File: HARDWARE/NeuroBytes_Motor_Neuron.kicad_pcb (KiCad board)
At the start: 2 copper layers, 51.2 x 28.4 mm, 28 parts, among them P1 JST_GH_4POS, P2 JST_GH_4POS, P3 JST_GH_4POS, P4 SERVO_CONN, P5 SERVO_CONN, P6 JST_GH_5-pos, Q1 MMBT3904, Q2 MMBT3904, Q3 MMBT3904, SW1 SW_PUSH, U1 STM32L011Gx, U2 LD3985G33R

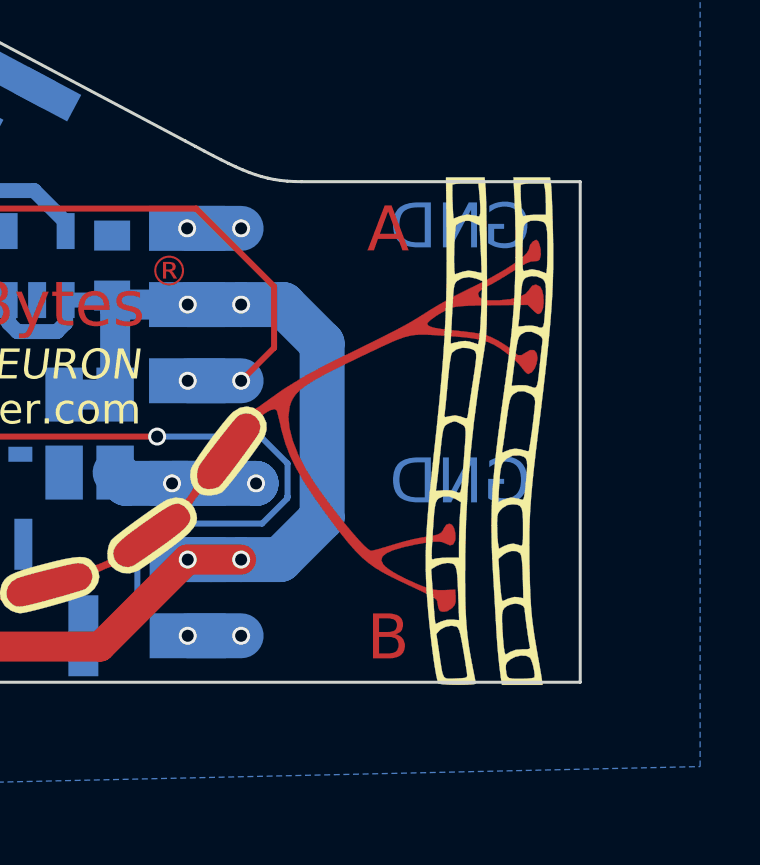
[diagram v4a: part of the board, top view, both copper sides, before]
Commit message: updated servo labels
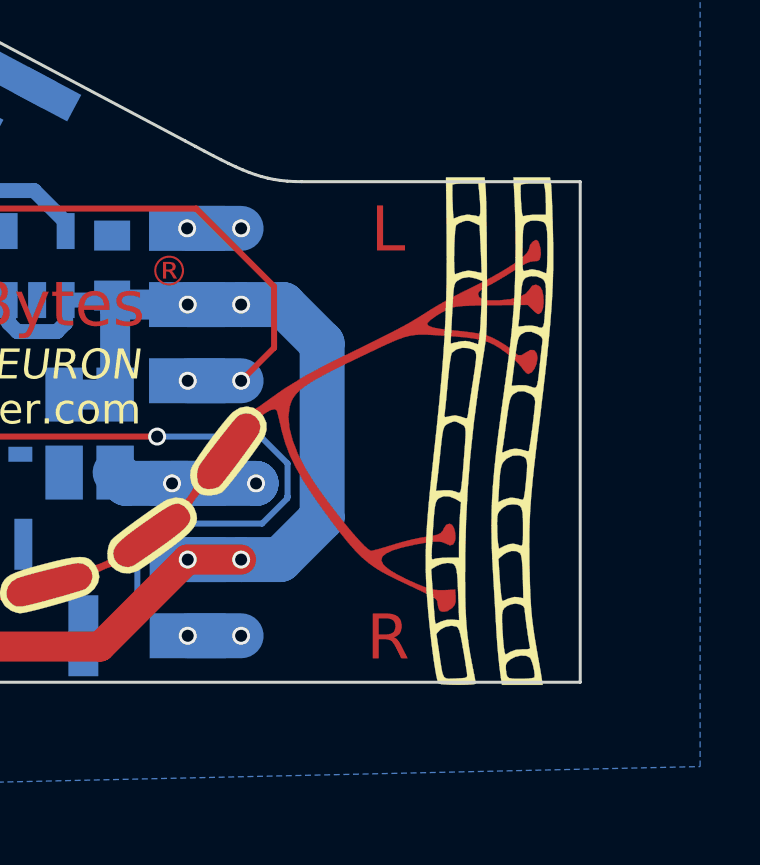
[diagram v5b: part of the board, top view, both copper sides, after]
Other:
- board text added: "BLK/BRN"
- board text added: "L"
- board text added: "LEFT SERVO"
- board text added: "R"
- board text added: "RIGHT SERVO"
- board text removed: "A"
- board text removed: "B"
- board text removed: "GND"
- board text removed: "SIG"
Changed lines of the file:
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@@
-(kicad_pcb (version 4) (host pcbnew 4.0.5-e0-6337~49~ubuntu14.04.1)
+(kicad_pcb (version 4) (host pcbnew 4.0.7-e1-6374~58~ubuntu14.04.1)
   (general
     (links 87)
@@
     (area 156.899999 38.899999 223.100001 76.780001)
     (thickness 1.6)
-    (drawings 129)
+    (drawings 127)
     (tracks 236)
     (zones 0)
@@
       (net 25 SERVO_2))
   )
+  (gr_text "RIGHT\nSERVO" (at 209.54 69.49) (layer B.SilkS)
+    (effects (font (size 1.5 1.5) (thickness 0.21)) (justify mirror))
+  )
+  (gr_text BLK/BRN (at 209.54 65.69) (layer B.Mask)
+    (effects (font (size 1 1) (thickness 0.14)) (justify mirror))
+  )
   (gr_text POWER (at 192.54 65.79) (layer B.SilkS)
     (effects (font (size 1.2 1.2) (thickness 0.17)) (justify mirror))
   )
   (gr_line (start 205.44 63.49) (end 205.44 64.39) (layer B.SilkS) (width 0.12))
-  (gr_line (start 205.44 63.99) (end 213.54 63.99) (layer B.SilkS) (width 0.12))
-  (gr_text SIG (at 209.94 62.19) (layer B.SilkS)
-    (effects (font (size 1.5 1.5) (thickness 0.21)) (justify mirror))
-  )
-  (gr_text SIG (at 209.94 70.79) (layer B.SilkS)
+  (gr_line (start 205.44 63.99) (end 213.54 63.99) (layer B.SilkS) (width 0.2))
+  (gr_text "LEFT\nSERVO" (at 209.54 60.89) (layer B.SilkS)
     (effects (font (size 1.5 1.5) (thickness 0.21)) (justify mirror))
   )
@@
     (effects (font (size 1 1) (thickness 0.14)))
   )
-  (gr_text GND (at 209.6 57.1) (layer B.Mask)
-    (effects (font (size 1.5 1.5) (thickness 0.21)) (justify mirror))
-  )
-  (gr_text GND (at 209.6 57.1) (layer B.Cu)
-    (effects (font (size 1.5 1.5) (thickness 0.21)) (justify mirror))
-  )
-  (gr_text GND (at 209.6 65.6) (layer B.Mask)
-    (effects (font (size 1.5 1.5) (thickness 0.21)) (justify mirror))
-  )
-  (gr_text GND (at 209.6 65.6) (layer B.Cu)
-    (effects (font (size 1.5 1.5) (thickness 0.21)) (justify mirror))
+  (gr_text BLK/BRN (at 209.54 57.19) (layer B.Mask)
+    (effects (font (size 1 1) (thickness 0.14)) (justify mirror))
   )
   (gr_line (start 207 55) (end 207 74.6) (layer Cmts.User) (width 0.12))
@@
     (effects (font (size 1.2 1.2) (thickness 0.17)) (justify mirror))
   )
-  (gr_text B (at 207.2 70.8) (layer F.Cu)
+  (gr_text R (at 207.2 70.8) (layer F.Cu)
     (effects (font (size 1.5 1.5) (thickness 0.21)))
   )
-  (gr_text A (at 207.2 57.2) (layer F.Cu)
+  (gr_text L (at 207.2 57.2) (layer F.Cu)
     (effects (font (size 1.5 1.5) (thickness 0.21)))
   )

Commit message: updated board graphics to reflect updated gear. other minor updates.
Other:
- board text added: "COMPONENT POSITION ORIGIN"
- board text added: "NOTES: 1. FOOTPRINTS ORIENTED PER IPC-7351FC LEVEL B (PIN 1 IN LOWER LEFT) 2. COMPONENT ROTATION IN DEGREES COUNTER-CLOCKWISE 3. ALL COMPONENTS MOUNTED ON B.CU LAYER (LED IS BOTTOM-MOUNT) 4. PCB IS 1.6mm FR4 RATED FOR ROHS REFLOW, 1OZ COPPER, ENIG FINISH 5. MATTE BLACK SOLDER MASK WITH WHITE SILKSCREEN 6. SOLDER PASTE MUST BE ROHS COMPLIANT (LEAD-FREE) 7. NO MARKS (E-TEST, QA, SERIAL NUMBER, ETC)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"
- board text added: "ROUTE BOARD OUTLINE EXCEPT FOR TWO ENDS"
- board text added: "V-SCORE PARALLEL ENDS"

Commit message: reloaded netlist. minor PCB changes.
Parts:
- C1, C4: value C -> 1u
- C2, C6, C7: value C -> 10u
- C3, C5: value C -> 0u1
- R1: value 220 -> 150
- R4: value R -> JMP
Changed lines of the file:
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@@
   (general
     (links 87)
-    (no_connects 0)
-    (area 155.44 35.09 252.297146 109.115)
+    (no_connects 1)
+    (area 162.385486 43.799953 213.653359 72.338769)
     (thickness 1.6)
     (drawings 156)
@@
     (mod_text_size 1 1)
     (mod_text_width 0.15)
-    (pad_size 1 2.7)
+    (pad_size 2 1)
     (pad_drill 0)
     (pad_to_mask_clearance 0)
@@
       (effects (font (size 1 1) (thickness 0.15)))
     )
-    (fp_text value C (at 0 4.7 90) (layer B.Fab) hide
+    (fp_text value 1u (at 0 4.7 90) (layer B.Fab) hide
       (effects (font (size 1 1) (thickness 0.15)) (justify mirror))
     )
@@
       (effects (font (size 1 1) (thickness 0.15)))
     )
-    (fp_text value C (at 0 1.5 135) (layer B.Fab) hide
+    (fp_text value 0u1 (at 0 1.5 135) (layer B.Fab) hide
       (effects (font (size 1 1) (thickness 0.15)) (justify mirror))
     )
@@
       (effects (font (size 1 1) (thickness 0.15)))
     )
-    (fp_text value C (at 0 1.5) (layer B.Fab) hide
+    (fp_text value 0u1 (at 0 1.5) (layer B.Fab) hide
       (effects (font (size 1 1) (thickness 0.15)) (justify mirror))
     )
@@
       (effects (font (size 1 1) (thickness 0.15)))
     )
-    (fp_text value 220 (at 0 1.5 180) (layer B.Fab) hide
+    (fp_text value 150 (at 0 1.5 180) (layer B.Fab) hide
       (effects (font (size 1 1) (thickness 0.15)) (justify mirror))
     )
@@
       (effects (font (size 1 1) (thickness 0.15)))
     )
-    (fp_text value R (at 0 1.5) (layer B.Fab) hide
+    (fp_text value JMP (at 0 1.5) (layer B.Fab) hide
       (effects (font (size 1 1) (thickness 0.15)) (justify mirror))
     )
@@
       (effects (font (size 1 1) (thickness 0.15)) (justify mirror))
     )
-    (fp_text value C (at 0 3.6 180) (layer B.Fab) hide
+    (fp_text value 10u (at 0 3.6 180) (layer B.Fab) hide
       (effects (font (size 1 1) (thickness 0.15)) (justify mirror))
     )
@@
       (effects (font (size 1 1) (thickness 0.15)) (justify mirror))
     )
-    (fp_text value C (at 0 4.7 270) (layer B.Fab) hide
+    (fp_text value 1u (at 0 4.7 270) (layer B.Fab) hide
       (effects (font (size 1 1) (thickness 0.15)) (justify mirror))
     )
@@
       (effects (font (size 1 1) (thickness 0.15)) (justify mirror))
     )
-    (fp_text value C (at 0 3.6 270) (layer B.Fab) hide
+    (fp_text value 10u (at 0 3.6 270) (layer B.Fab) hide
       (effects (font (size 1 1) (thickness 0.15)) (justify mirror))
     )
@@
       (effects (font (size 1 1) (thickness 0.15)) (justify mirror))
     )
-    (fp_text value C (at 0 3.6 270) (layer B.Fab) hide
+    (fp_text value 10u (at 0 3.6 270) (layer B.Fab) hide
       (effects (font (size 1 1) (thickness 0.15)) (justify mirror))
     )
@@
   (module KiCad_Footprints:ZF_CONN_SERVO_HDR_SMT (layer B.Cu)
     (at 200.5 59.7)
+    (attr smd)
     (fp_text reference P4 (at 0 -4.445) (layer B.Fab)
       (effects (font (size 1 1) (thickness 0.15)) (justify mirror))
@@
   (module KiCad_Footprints:ZF_CONN_SERVO_HDR_SMT (layer B.Cu)
     (at 200.52 68.2)
+    (attr smd)
     (fp_text reference P5 (at 0 -4.445) (layer B.Fab)
       (effects (font (size 1 1) (thickness 0.15)) (justify mirror))
@@
   (module KiCad_Footprints:ZF_LOGO_Motor_Neuron (layer F.Cu)
     (at 177 57.95)
+    (attr smd)
     (fp_text reference G*** (at 0 0) (layer F.SilkS) hide
       (effects (font (thickness 0.3)))
